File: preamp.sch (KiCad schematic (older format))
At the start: 44 parts, among them P1 CONN_01X04, P2 CONN_01X02, P3 CONN_01X04, T1 TRANSFO2, U1 OPA137N, U2 LM7815CT, U3 LM7915CT, U4 OPA137N

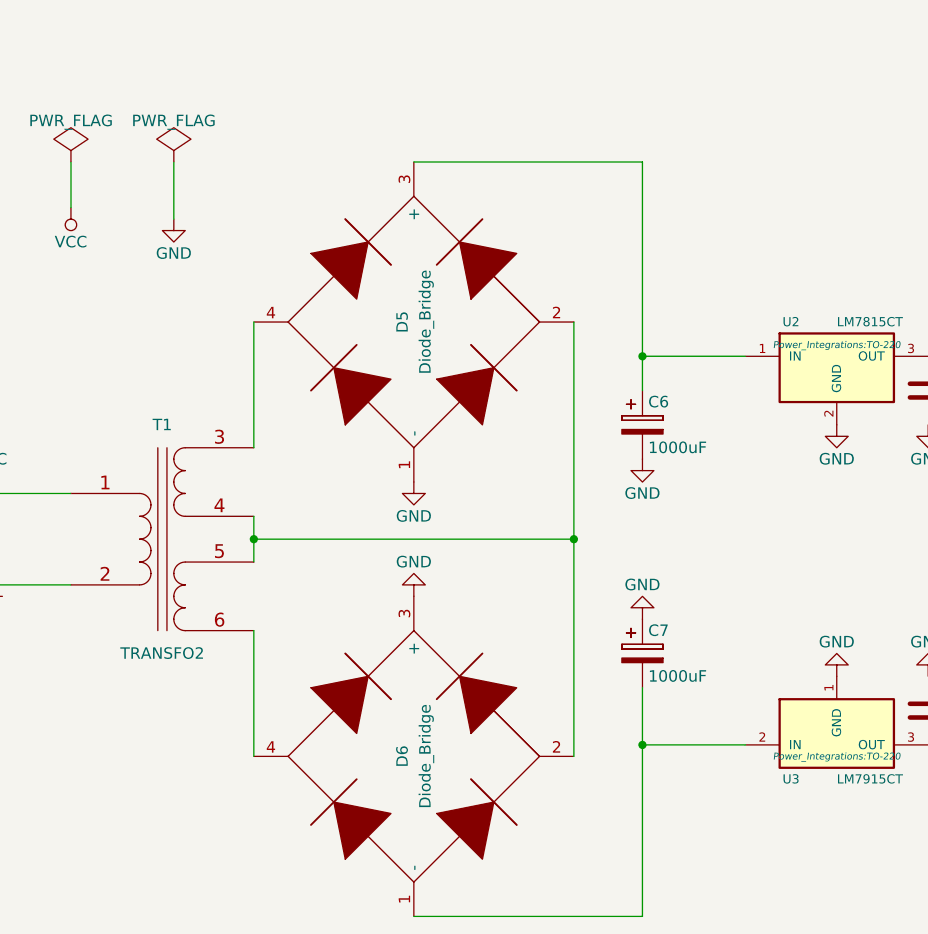
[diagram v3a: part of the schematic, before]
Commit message: Finish adding PSU and second channel.  Ready for fab?
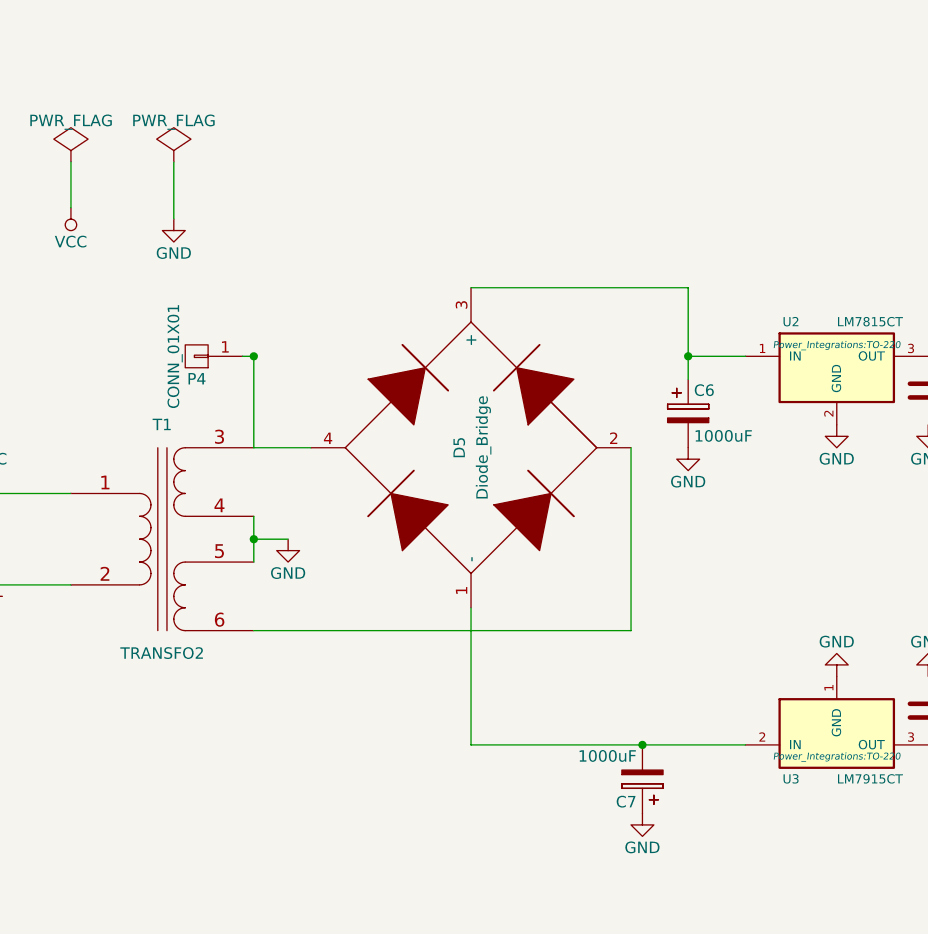
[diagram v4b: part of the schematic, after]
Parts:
- removed D6: Diode_Bridge, preamp:Bridge-Rectifier-SOIC-4, symbol Diode_Bridge
- added P4: CONN_01X01, Pin_Headers:Pin_Header_Straight_1x01, symbol CONN_01X01
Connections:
- net GND: now also T1.4 (SB), T1.5 (SC); no longer D5.1 (-)
- net at D5.4, T1.3 (SA): now also P4.1 (P1)
- net at T1.6 (SD): now also D5.2
- net at C7.2, U3.2 (IN): now also D5.1 (-)
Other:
- moved on the sheet: C6, C7, D5
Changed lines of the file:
@@
 $EndComp
 $Comp
-L -15V #PWR20
+L -15V #PWR21
 U 1 1 5574943C
 P 7000 1350
-F 0 "#PWR20" H 7000 1450 50  0001 C CNN
+F 0 "#PWR21" H 7000 1450 50  0001 C CNN
 F 1 "-15V" H 7000 1500 50  0000 C CNN
 F 2 "" H 7000 1350 60  0000 C CNN
@@
 $EndComp
 $Comp
-L -15V #PWR16
+L -15V #PWR17
 U 1 1 557494A4
 P 6550 1850
-F 0 "#PWR16" H 6550 1950 50  0001 C CNN
+F 0 "#PWR17" H 6550 1950 50  0001 C CNN
 F 1 "-15V" H 6550 2000 50  0000 C CNN
 F 2 "" H 6550 1850 60  0000 C CNN
@@
 $EndComp
 $Comp
-L -15V #PWR27
+L -15V #PWR28
 U 1 1 557494E8
 P 8150 2100
-F 0 "#PWR27" H 8150 2200 50  0001 C CNN
+F 0 "#PWR28" H 8150 2200 50  0001 C CNN
 F 1 "-15V" H 8150 2250 50  0000 C CNN
 F 2 "" H 8150 2100 60  0000 C CNN
@@
 $EndComp
 $Comp
-L -15V #PWR22
+L -15V #PWR23
 U 1 1 557A9B89
 P 7000 4200
-F 0 "#PWR22" H 7000 4300 50  0001 C CNN
+F 0 "#PWR23" H 7000 4300 50  0001 C CNN
 F 1 "-15V" H 7000 4350 50  0000 C CNN
 F 2 "" H 7000 4200 60  0000 C CNN
@@
 $EndComp
 $Comp
-L -15V #PWR18
+L -15V #PWR19
 U 1 1 557A9B95
 P 6550 4700
-F 0 "#PWR18" H 6550 4800 50  0001 C CNN
+F 0 "#PWR19" H 6550 4800 50  0001 C CNN
 F 1 "-15V" H 6550 4850 50  0000 C CNN
 F 2 "" H 6550 4700 60  0000 C CNN
@@
 $EndComp
 $Comp
-L -15V #PWR28
+L -15V #PWR29
 U 1 1 557A9B9B
 P 8150 4950
-F 0 "#PWR28" H 8150 5050 50  0001 C CNN
+F 0 "#PWR29" H 8150 5050 50  0001 C CNN
 F 1 "-15V" H 8150 5100 50  0000 C CNN
 F 2 "" H 8150 4950 60  0000 C CNN
@@
 L Diode_Bridge D5
 U 1 1 557AA43E
-P 3050 5000
-F 0 "D5" H 3050 5050 50  0000 C CNN
-F 1 "Diode_Bridge" H 3050 4950 50  0000 C CNN
-F 2 "preamp:Bridge-Rectifier-SOIC-4" H 3050 5000 60  0001 C CNN
-F 3 "" H 3050 5000 60  0000 C CNN
-	1    3050 5000
-	0    -1   -1   0
-$EndComp
-$Comp
-L Diode_Bridge D6
-U 1 1 557AA650
-P 3050 6900
-F 0 "D6" H 3050 6950 50  0000 C CNN
-F 1 "Diode_Bridge" H 3050 6850 50  0000 C CNN
-F 2 "preamp:Bridge-Rectifier-SOIC-4" H 3050 6900 60  0001 C CNN
-F 3 "" H 3050 6900 60  0000 C CNN
-	1    3050 6900
+P 3300 5550
+F 0 "D5" H 3300 5600 50  0000 C CNN
+F 1 "Diode_Bridge" H 3300 5500 50  0000 C CNN
+F 2 "preamp:Bridge-Rectifier-SOIC-4" H 3300 5550 60  0001 C CNN
+F 3 "" H 3300 5550 60  0000 C CNN
+	1    3300 5550
 	0    -1   -1   0
 $EndComp
@@
 L CP C6
 U 1 1 557AC5AE
-P 4050 5450
-F 0 "C6" H 4075 5550 50  0000 L CNN
-F 1 "1000uF" H 4075 5350 50  0000 L CNN
-F 2 "Capacitors_Elko_ThroughHole:Elko_vert_20x10mm_RM7.5" H 4088 5300 30  0001 C CNN
-F 3 "" H 4050 5450 60  0000 C CNN
-	1    4050 5450
+P 4250 5400
+F 0 "C6" H 4275 5500 50  0000 L CNN
+F 1 "1000uF" H 4275 5300 50  0000 L CNN
+F 2 "Capacitors_Elko_ThroughHole:Elko_vert_20x10mm_RM7.5" H 4288 5250 30  0001 C CNN
+F 3 "" H 4250 5400 60  0000 C CNN
+	1    4250 5400
 	1    0    0    -1
 $EndComp
@@
 L CP C7
 U 1 1 557AC609
-P 4050 6450
-F 0 "C7" H 4075 6550 50  0000 L CNN
-F 1 "1000uF" H 4075 6350 50  0000 L CNN
-F 2 "Capacitors_Elko_ThroughHole:Elko_vert_20x10mm_RM7.5" H 4088 6300 30  0001 C CNN
-F 3 "" H 4050 6450 60  0000 C CNN
-	1    4050 6450
-	1    0    0    -1
+P 4050 7000
+F 0 "C7" H 4075 7100 50  0000 L CNN
+F 1 "1000uF" H 4075 6900 50  0000 L CNN
+F 2 "Capacitors_Elko_ThroughHole:Elko_vert_20x10mm_RM7.5" H 4088 6850 30  0001 C CNN
+F 3 "" H 4050 7000 60  0000 C CNN
+	1    4050 7000
+	-1   0    0    1
 $EndComp
 $Comp
@@
 $EndComp
 $Comp
-L GND #PWR014
-U 1 1 557ACE90
-P 3050 5700
-F 0 "#PWR014" H 3050 5450 50  0001 C CNN
-F 1 "GND" H 3050 5550 50  0000 C CNN
-F 2 "" H 3050 5700 60  0000 C CNN
-F 3 "" H 3050 5700 60  0000 C CNN
-	1    3050 5700
-	1    0    0    -1
-$EndComp
-$Comp
-L GND #PWR015
-U 1 1 557ACEFA
-P 3050 6200
-F 0 "#PWR015" H 3050 5950 50  0001 C CNN
-F 1 "GND" H 3050 6050 50  0000 C CNN
-F 2 "" H 3050 6200 60  0000 C CNN
-F 3 "" H 3050 6200 60  0000 C CNN
-	1    3050 6200
-	-1   0    0    1
-$EndComp
-$Comp
 L GND #PWR016
 U 1 1 557ACF39
-P 4050 5600
-F 0 "#PWR016" H 4050 5350 50  0001 C CNN
-F 1 "GND" H 4050 5450 50  0000 C CNN
-F 2 "" H 4050 5600 60  0000 C CNN
-F 3 "" H 4050 5600 60  0000 C CNN
-	1    4050 5600
+P 4250 5550
+F 0 "#PWR016" H 4250 5300 50  0001 C CNN
+F 1 "GND" H 4250 5400 50  0000 C CNN
+F 2 "" H 4250 5550 60  0000 C CNN
+F 3 "" H 4250 5550 60  0000 C CNN
+	1    4250 5550
 	1    0    0    -1
 $EndComp
@@
 $EndComp
 $Comp
-L -15V #PWR14
+L -15V #PWR15
 U 1 1 557AD74C
 P 5650 6850
-F 0 "#PWR14" H 5650 6950 50  0001 C CNN
+F 0 "#PWR15" H 5650 6950 50  0001 C CNN
 F 1 "-15V" H 5650 7000 50  0000 C CNN
 F 2 "" H 5650 6850 60  0000 C CNN
@@
 L GND #PWR030
 U 1 1 557E6C53
-P 4050 6300
-F 0 "#PWR030" H 4050 6050 50  0001 C CNN
-F 1 "GND" H 4050 6150 50  0000 C CNN
-F 2 "" H 4050 6300 60  0000 C CNN
-F 3 "" H 4050 6300 60  0000 C CNN
-	1    4050 6300
-	-1   0    0    1
+P 4050 7150
+F 0 "#PWR030" H 4050 6900 50  0001 C CNN
+F 1 "GND" H 4050 7000 50  0000 C CNN
+F 2 "" H 4050 7150 60  0000 C CNN
+F 3 "" H 4050 7150 60  0000 C CNN
+	1    4050 7150
+	1    0    0    -1
 $EndComp
 $Comp
@@
 Wire Wire Line
 	2350 5850 2350 6050
-Wire Wire Line
-	3750 5000 3750 6900
-Wire Wire Line
-	2350 5550 2350 5000
-Wire Wire Line
-	2350 5950 3750 5950
-Connection ~ 3750 5950
 Connection ~ 2350 5950
 Wire Wire Line
-	4050 4300 4050 5300
-Wire Wire Line
-	4050 7600 3050 7600
-Wire Wire Line
-	4050 6600 4050 7600
-Wire Wire Line
-	4500 5150 4050 5150
-Connection ~ 4050 5150
-Wire Wire Line
-	4500 6850 4050 6850
+	4500 5150 4250 5150
+Wire Wire Line
+	3300 6850 4500 6850
 Connection ~ 4050 6850
 Wire Wire Line
@@
 Wire Wire Line
 	5300 6850 5650 6850
-Wire Wire Line
-	3050 4300 4050 4300
 Wire Wire Line
 	1200 5900 1200 5750
@@
 Connection ~ 10650 3100
 Wire Wire Line
-	2350 6900 2350 6350
-Wire Wire Line
 	7250 2350 7250 2100
 Wire Wire Line
 	2000 4300 2000 4550
+$Comp
+L CONN_01X01 P4
+U 1 1 558063EE
+P 2100 5150
+F 0 "P4" H 2100 5250 50  0000 C CNN
+F 1 "CONN_01X01" V 2200 5150 50  0000 C CNN
+F 2 "Pin_Headers:Pin_Header_Straight_1x01" H 2100 5150 60  0001 C CNN
+F 3 "" H 2100 5150 60  0000 C CNN
+	1    2100 5150
+	-1   0    0    1
+$EndComp
+Wire Wire Line
+	2350 6350 4000 6350
+Wire Wire Line
+	4000 6350 4000 5550
+Wire Wire Line
+	3300 6250 3300 6850
+$Comp
+L GND #PWR?
+U 1 1 558082FD
+P 2500 5950
+F 0 "#PWR?" H 2500 5700 50  0001 C CNN
+F 1 "GND" H 2500 5800 50  0000 C CNN
+F 2 "" H 2500 5950 60  0000 C CNN
+F 3 "" H 2500 5950 60  0000 C CNN
+	1    2500 5950
+	1    0    0    -1
+$EndComp
+Wire Wire Line
+	2350 5950 2500 5950
+Wire Wire Line
+	2300 5150 2350 5150
+Connection ~ 2350 5150
+Wire Wire Line
+	4250 4850 4250 5250
+Connection ~ 4250 5150
+Wire Wire Line
+	2350 5150 2350 5550
+Wire Wire Line
+	2350 5550 2600 5550
+Wire Wire Line
+	3300 4850 4250 4850
 $EndSCHEMATC

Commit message: Cleanup a label I missed
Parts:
- T1: footprint preamp:preamp_transformer_6pin -> preamp:preamp_transformer_6pin_half
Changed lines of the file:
@@
 $EndComp
 $Comp
-L -15V #PWR21
+L -15V #PWR20
 U 1 1 5574943C
 P 7000 1350
-F 0 "#PWR21" H 7000 1450 50  0001 C CNN
+F 0 "#PWR20" H 7000 1450 50  0001 C CNN
 F 1 "-15V" H 7000 1500 50  0000 C CNN
 F 2 "" H 7000 1350 60  0000 C CNN
@@
 $EndComp
 $Comp
-L -15V #PWR17
+L -15V #PWR16
 U 1 1 557494A4
 P 6550 1850
-F 0 "#PWR17" H 6550 1950 50  0001 C CNN
+F 0 "#PWR16" H 6550 1950 50  0001 C CNN
 F 1 "-15V" H 6550 2000 50  0000 C CNN
 F 2 "" H 6550 1850 60  0000 C CNN
@@
 $EndComp
 $Comp
-L -15V #PWR28
+L -15V #PWR27
 U 1 1 557494E8
 P 8150 2100
-F 0 "#PWR28" H 8150 2200 50  0001 C CNN
+F 0 "#PWR27" H 8150 2200 50  0001 C CNN
 F 1 "-15V" H 8150 2250 50  0000 C CNN
 F 2 "" H 8150 2100 60  0000 C CNN
@@
 $EndComp
 $Comp
-L -15V #PWR23
+L -15V #PWR22
 U 1 1 557A9B89
 P 7000 4200
-F 0 "#PWR23" H 7000 4300 50  0001 C CNN
+F 0 "#PWR22" H 7000 4300 50  0001 C CNN
 F 1 "-15V" H 7000 4350 50  0000 C CNN
 F 2 "" H 7000 4200 60  0000 C CNN
@@
 $EndComp
 $Comp
-L -15V #PWR19
+L -15V #PWR18
 U 1 1 557A9B95
 P 6550 4700
-F 0 "#PWR19" H 6550 4800 50  0001 C CNN
+F 0 "#PWR18" H 6550 4800 50  0001 C CNN
 F 1 "-15V" H 6550 4850 50  0000 C CNN
 F 2 "" H 6550 4700 60  0000 C CNN
@@
 $EndComp
 $Comp
-L -15V #PWR29
+L -15V #PWR28
 U 1 1 557A9B9B
 P 8150 4950
-F 0 "#PWR29" H 8150 5050 50  0001 C CNN
+F 0 "#PWR28" H 8150 5050 50  0001 C CNN
 F 1 "-15V" H 8150 5100 50  0000 C CNN
 F 2 "" H 8150 4950 60  0000 C CNN
@@
 F 0 "T1" H 1950 6450 50  0000 C CNN
 F 1 "TRANSFO2" H 1950 5450 50  0000 C CNN
-F 2 "preamp:preamp_transformer_6pin" H 1950 5950 60  0001 C CNN
+F 2 "preamp:preamp_transformer_6pin_half" H 1950 5950 60  0001 C CNN
 F 3 "" H 1950 5950 60  0000 C CNN
 	1    1950 5950
@@
 $EndComp
 $Comp
-L GND #PWR016
+L GND #PWR014
 U 1 1 557ACF39
 P 4250 5550
-F 0 "#PWR016" H 4250 5300 50  0001 C CNN
+F 0 "#PWR014" H 4250 5300 50  0001 C CNN
 F 1 "GND" H 4250 5400 50  0000 C CNN
 F 2 "" H 4250 5550 60  0000 C CNN
@@
 $EndComp
 $Comp
-L GND #PWR017
+L GND #PWR015
 U 1 1 557ACFF6
 P 4900 6550
-F 0 "#PWR017" H 4900 6300 50  0001 C CNN
+F 0 "#PWR015" H 4900 6300 50  0001 C CNN
 F 1 "GND" H 4900 6400 50  0000 C CNN
 F 2 "" H 4900 6550 60  0000 C CNN
@@
 $EndComp
 $Comp
-L GND #PWR018
+L GND #PWR016
 U 1 1 557AD598
 P 5300 5450
-F 0 "#PWR018" H 5300 5200 50  0001 C CNN
+F 0 "#PWR016" H 5300 5200 50  0001 C CNN
 F 1 "GND" H 5300 5300 50  0000 C CNN
 F 2 "" H 5300 5450 60  0000 C CNN
@@
 $EndComp
 $Comp
-L GND #PWR019
+L GND #PWR017
 U 1 1 557AD5D9
 P 5300 6550
-F 0 "#PWR019" H 5300 6300 50  0001 C CNN
+F 0 "#PWR017" H 5300 6300 50  0001 C CNN
 F 1 "GND" H 5300 6400 50  0000 C CNN
 F 2 "" H 5300 6550 60  0000 C CNN
@@
 $EndComp
 $Comp
-L -15V #PWR15
+L -15V #PWR14
 U 1 1 557AD74C
 P 5650 6850
-F 0 "#PWR15" H 5650 6950 50  0001 C CNN
+F 0 "#PWR14" H 5650 6950 50  0001 C CNN
 F 1 "-15V" H 5650 7000 50  0000 C CNN
 F 2 "" H 5650 6850 60  0000 C CNN
@@
 $EndComp
 $Comp
-L +15V #PWR020
+L +15V #PWR018
 U 1 1 557AD78D
 P 5650 5150
-F 0 "#PWR020" H 5650 5000 50  0001 C CNN
+F 0 "#PWR018" H 5650 5000 50  0001 C CNN
 F 1 "+15V" H 5650 5290 50  0000 C CNN
 F 2 "" H 5650 5150 60  0000 C CNN
@@
 $EndComp
 $Comp
-L Earth #PWR021
+L Earth #PWR019
 U 1 1 557ADF9C
 P 1200 6150
-F 0 "#PWR021" H 1200 5900 50  0001 C CNN
+F 0 "#PWR019" H 1200 5900 50  0001 C CNN
 F 1 "Earth" H 1200 6000 50  0001 C CNN
 F 2 "" H 1200 6150 60  0000 C CNN
@@
 $EndComp
 $Comp
-L VCC #PWR022
+L VCC #PWR020
 U 1 1 557ADFDE
 P 1200 5750
-F 0 "#PWR022" H 1200 5600 50  0001 C CNN
+F 0 "#PWR020" H 1200 5600 50  0001 C CNN
 F 1 "VCC" H 1200 5900 50  0000 C CNN
 F 2 "" H 1200 5750 60  0000 C CNN
@@
 $EndComp
 $Comp
-L PWR_FLAG #FLG023
+L PWR_FLAG #FLG021
 U 1 1 557AE04E
 P 1050 4300
-F 0 "#FLG023" H 1050 4395 50  0001 C CNN
+F 0 "#FLG021" H 1050 4395 50  0001 C CNN
 F 1 "PWR_FLAG" H 1050 4480 50  0000 C CNN
 F 2 "" H 1050 4300 60  0000 C CNN
@@
 $EndComp
 $Comp
-L PWR_FLAG #FLG024
+L PWR_FLAG #FLG022
 U 1 1 557AE090
 P 1550 4300
-F 0 "#FLG024" H 1550 4395 50  0001 C CNN
+F 0 "#FLG022" H 1550 4395 50  0001 C CNN
 F 1 "PWR_FLAG" H 1550 4480 50  0000 C CNN
 F 2 "" H 1550 4300 60  0000 C CNN
@@
 $EndComp
 $Comp
-L Earth #PWR025
+L Earth #PWR023
 U 1 1 557AE112
 P 1050 4500
-F 0 "#PWR025" H 1050 4250 50  0001 C CNN
+F 0 "#PWR023" H 1050 4250 50  0001 C CNN
 F 1 "Earth" H 1050 4350 50  0001 C CNN
 F 2 "" H 1050 4500 60  0000 C CNN
@@
 $EndComp
 $Comp
-L VCC #PWR026
+L VCC #PWR024
 U 1 1 557AE154
 P 1550 4500
-F 0 "#PWR026" H 1550 4350 50  0001 C CNN
+F 0 "#PWR024" H 1550 4350 50  0001 C CNN
 F 1 "VCC" H 1550 4650 50  0000 C CNN
 F 2 "" H 1550 4500 60  0000 C CNN
@@
 $EndComp
 $Comp
-L GND #PWR027
+L GND #PWR025
 U 1 1 557E25A0
 P 10650 3500
-F 0 "#PWR027" H 10650 3250 50  0001 C CNN
+F 0 "#PWR025" H 10650 3250 50  0001 C CNN
 F 1 "GND" H 10650 3350 50  0000 C CNN
 F 2 "" H 10650 3500 60  0000 C CNN
@@
 NoConn ~ 9600 5950
 $Comp
-L GND #PWR028
+L GND #PWR026
 U 1 1 557E5A9A
 P 4900 5450
-F 0 "#PWR028" H 4900 5200 50  0001 C CNN
+F 0 "#PWR026" H 4900 5200 50  0001 C CNN
 F 1 "GND" H 4900 5300 50  0000 C CNN
 F 2 "" H 4900 5450 60  0000 C CNN
@@
 $EndComp
 $Comp
-L GND #PWR029
+L GND #PWR027
 U 1 1 557E632B
 P 7250 2350
-F 0 "#PWR029" H 7250 2100 50  0001 C CNN
+F 0 "#PWR027" H 7250 2100 50  0001 C CNN
 F 1 "GND" H 7250 2200 50  0000 C CNN
 F 2 "" H 7250 2350 60  0000 C CNN
@@
 $EndComp
 $Comp
-L GND #PWR030
+L GND #PWR028
 U 1 1 557E6C53
 P 4050 7150
-F 0 "#PWR030" H 4050 6900 50  0001 C CNN
+F 0 "#PWR028" H 4050 6900 50  0001 C CNN
 F 1 "GND" H 4050 7000 50  0000 C CNN
 F 2 "" H 4050 7150 60  0000 C CNN
@@
 $EndComp
 $Comp
-L GND #PWR031
+L GND #PWR029
 U 1 1 557E7348
 P 2000 4550
-F 0 "#PWR031" H 2000 4300 50  0001 C CNN
+F 0 "#PWR029" H 2000 4300 50  0001 C CNN
 F 1 "GND" H 2000 4400 50  0000 C CNN
 F 2 "" H 2000 4550 60  0000 C CNN
@@
 $EndComp
 $Comp
-L PWR_FLAG #FLG032
+L PWR_FLAG #FLG030
 U 1 1 557E7388
 P 2000 4300
-F 0 "#FLG032" H 2000 4395 50  0001 C CNN
+F 0 "#FLG030" H 2000 4395 50  0001 C CNN
 F 1 "PWR_FLAG" H 2000 4480 50  0000 C CNN
 F 2 "" H 2000 4300 60  0000 C CNN
@@
 	3300 6250 3300 6850
 $Comp
-L GND #PWR?
+L GND #PWR031
 U 1 1 558082FD
 P 2500 5950
-F 0 "#PWR?" H 2500 5700 50  0001 C CNN
+F 0 "#PWR031" H 2500 5700 50  0001 C CNN
 F 1 "GND" H 2500 5800 50  0000 C CNN
 F 2 "" H 2500 5950 60  0000 C CNN
